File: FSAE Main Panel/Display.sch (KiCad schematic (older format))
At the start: 66 parts, among them U501 TLC6C598, U502 TLC6C5816, U503 TLC6C5816, U504 TLC6C5816

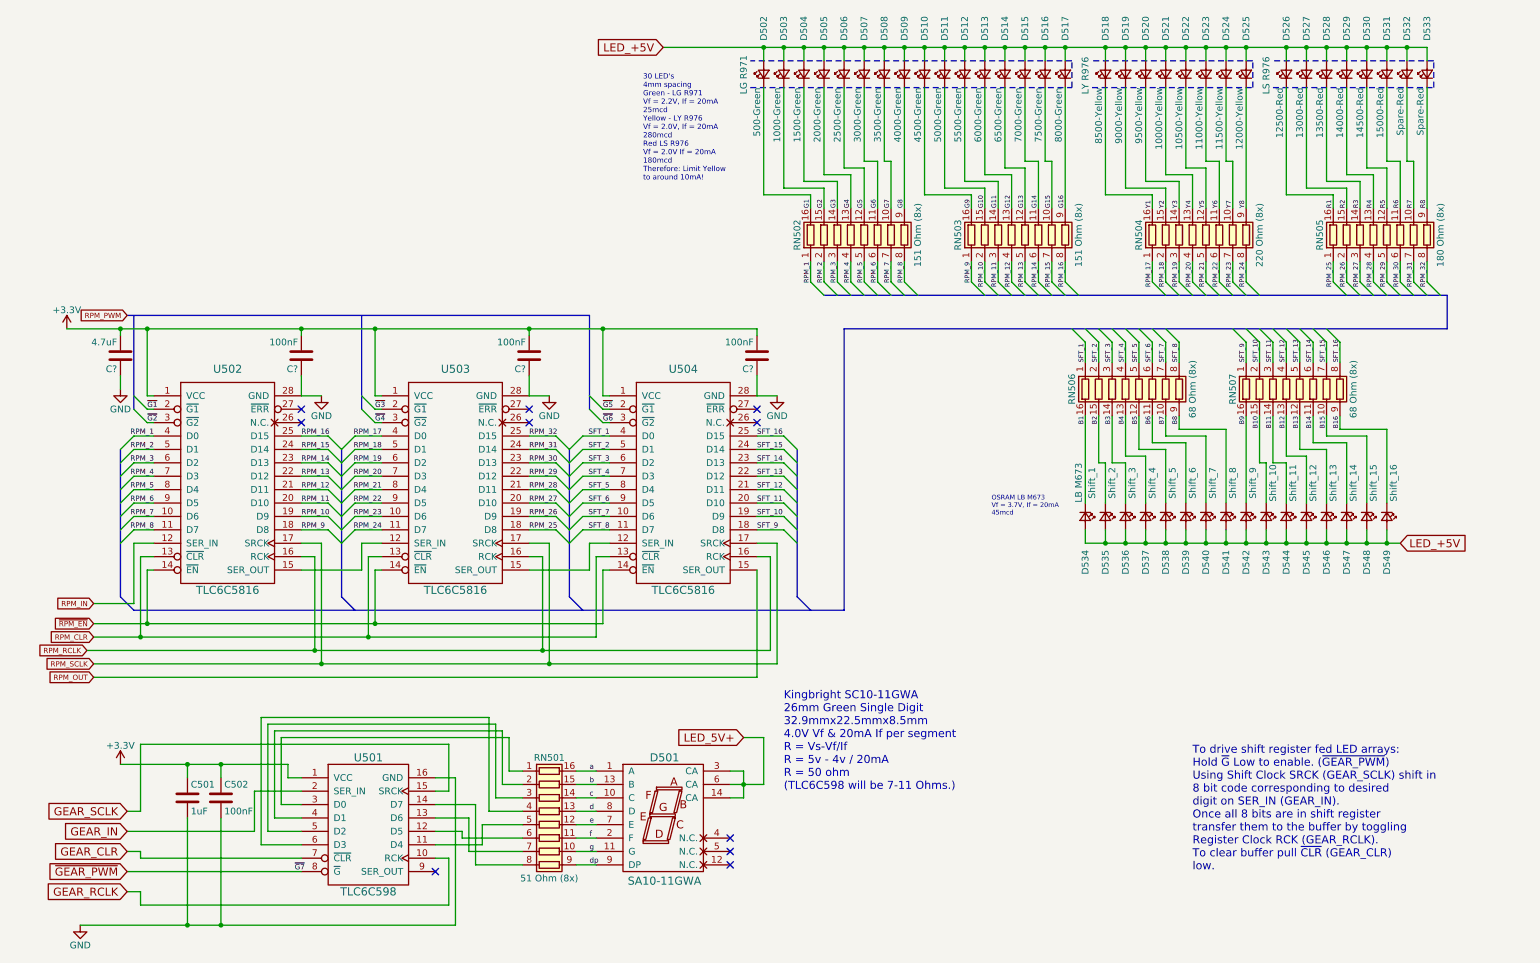
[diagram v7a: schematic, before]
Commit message: Added power regulator for LEDs, further GPIO considerations
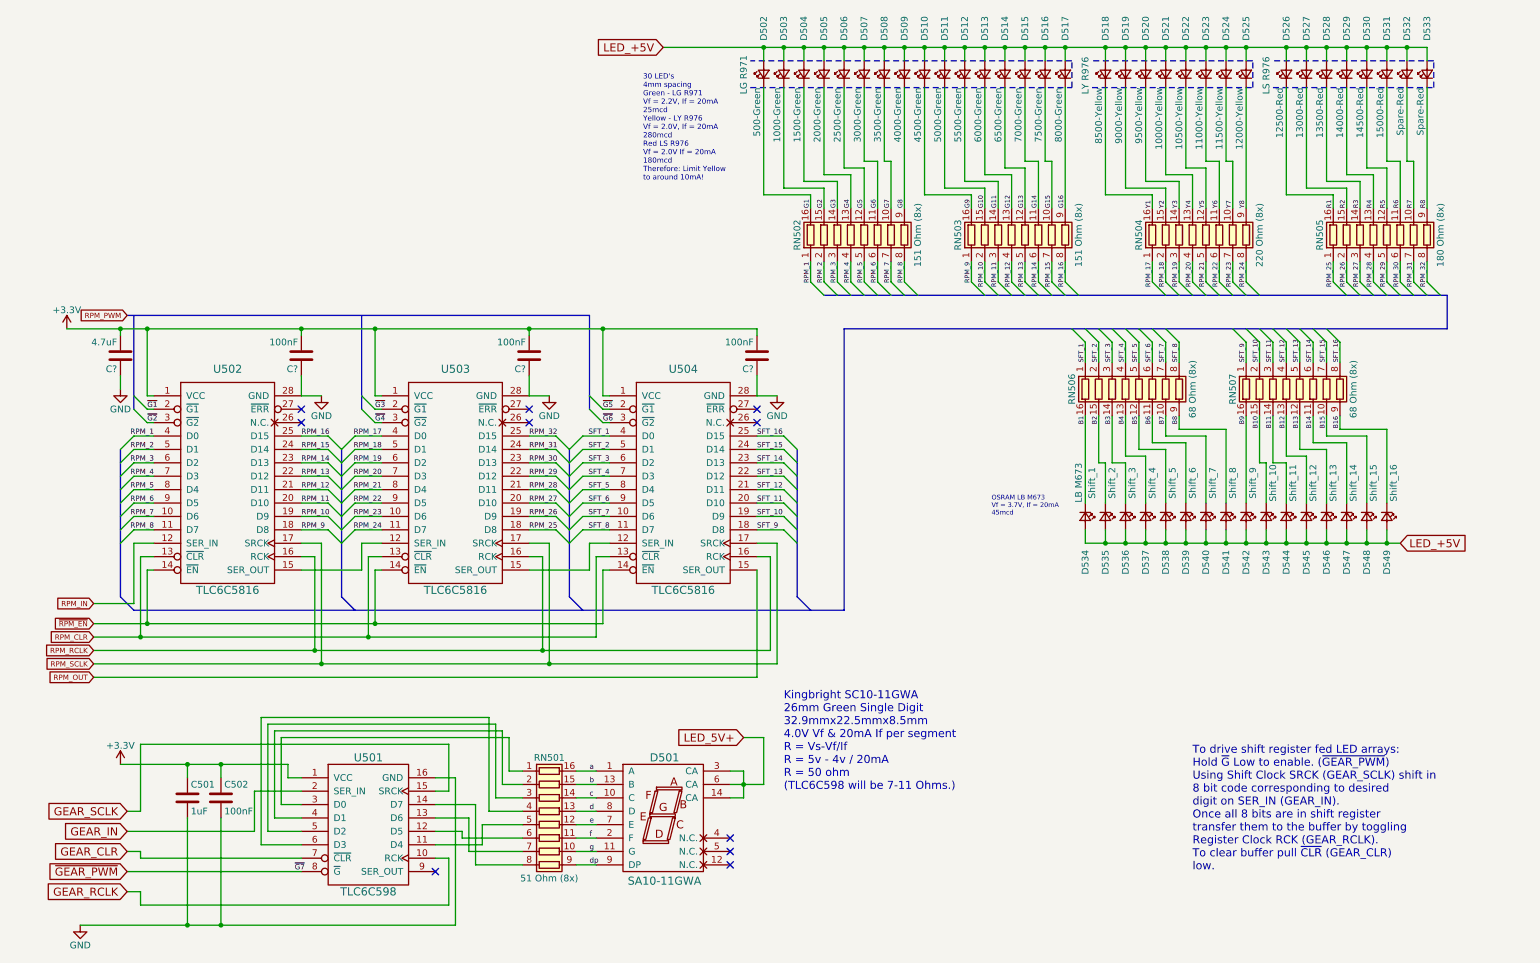
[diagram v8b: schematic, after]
